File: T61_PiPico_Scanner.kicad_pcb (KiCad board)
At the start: 2 copper layers, 60 x 45 mm, 36 parts, among them J101 GND, J102 VBUS, J103 EXT5V, J105 GND, J106 PWRSWITCH, J107 AA01B-S040VA1, Q101 2N7002, Q102 2N7002, Q103 DMG2305UX, U101 Pico

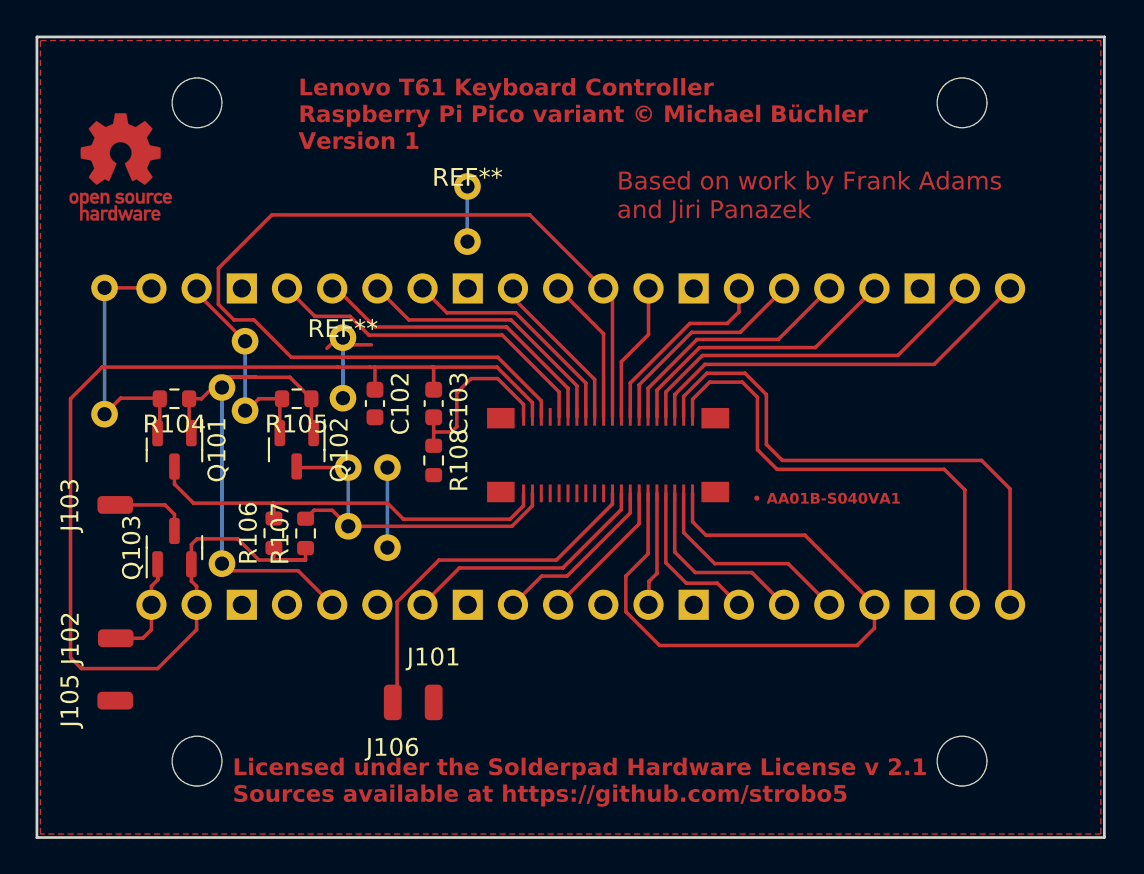
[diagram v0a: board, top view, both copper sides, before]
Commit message: rev 1.1: swap PS/2 clk and data for QMK's RP2040 PIO implementation
The only two boards with the wrong order were fixed manually.
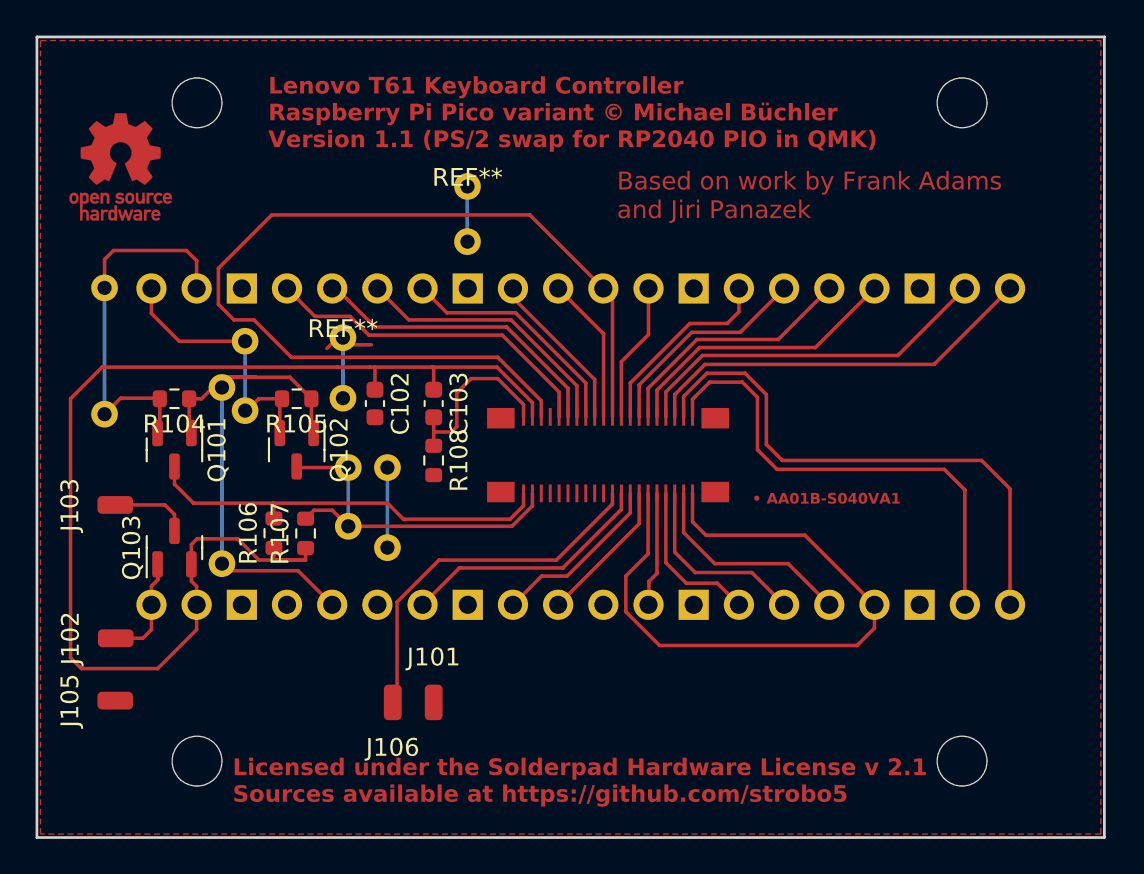
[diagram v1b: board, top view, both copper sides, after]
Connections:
- U101 pad 1: /TP4CLK_3V3 -> /TP4DATA_3V3
- U101 pad 2: /TP4DATA_3V3 -> /TP4CLK_3V3
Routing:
- net /TP4CLK_3V3: track 15.1 -> 21.8 mm
- net /TP4DATA_3V3: track 12.3 -> 16.0 mm
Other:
- board text added: "Lenovo T61 Keyboard Controller Raspberry Pi Pico variant © Michael Büchler Version 1.1 (PS/2 swap for RP2040 PIO in QMK)"
- board text removed: "Lenovo T61 Keyboard Controller Raspberry Pi Pico variant © Michael Büchler Version 1"
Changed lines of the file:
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@@
       (stroke (width 0.12) (type solid)) (layer "B.Fab"))
     (pad "1" thru_hole oval (at -8.89 24.13 270) (size 1.7 1.7) (drill 1.02) (layers "*.Cu" "*.Mask")
-      (net 41 "/TP4CLK_3V3") (pinfunction "GPIO0") (pintype "bidirectional"))
+      (net 42 "/TP4DATA_3V3") (pinfunction "GPIO0") (pintype "bidirectional"))
     (pad "2" thru_hole oval (at -8.89 21.59 270) (size 1.7 1.7) (drill 1.02) (layers "*.Cu" "*.Mask")
-      (net 42 "/TP4DATA_3V3") (pinfunction "GPIO1") (pintype "bidirectional"))
+      (net 41 "/TP4CLK_3V3") (pinfunction "GPIO1") (pintype "bidirectional"))
     (pad "3" thru_hole rect (at -8.89 19.05 270) (size 1.7 1.7) (drill 1.02) (layers "*.Cu" "*.Mask")
       (net 5 "GND") (pinfunction "GND") (pintype "power_in"))
@@
   (gr_line (start 118 128.295358) (end 118 83.295358)
     (stroke (width 0.1524) (type solid)) (layer "Edge.Cuts"))
-  (gr_text "Lenovo T61 Keyboard Controller\nRaspberry Pi Pico variant © Michael Büchler\nVersion 1" (at 132.7 89.7) (layer "F.Cu" knockout)
+  (gr_text "Lenovo T61 Keyboard Controller\nRaspberry Pi Pico variant © Michael Büchler\nVersion 1.1 (PS/2 swap for RP2040 PIO in QMK)" (at 131 89.6) (layer "F.Cu" knockout)
     (effects (font (size 0.93472 0.93472) (thickness 0.186944) bold) (justify left bottom))
   )
@@
   (segment (start 133.425 103.632) (end 132.218 102.425) (width 0.2) (layer "F.Cu") (net 40))
   (segment (start 128.4 112.9) (end 128.4 103) (width 0.2) (layer "B.Cu") (net 40))
-  (segment (start 123.90004 97.4) (end 124.18427 97.68423) (width 0.2) (layer "F.Cu") (net 41))
+  (segment (start 126.976 97.676) (end 126.976 97.4325) (width 0.2) (layer "F.Cu") (net 41))
   (segment (start 124.905 105.442) (end 124.905 103.632) (width 0.2) (layer "F.Cu") (net 41))
   (segment (start 121.8 104.5) (end 122.7 103.6) (width 0.2) (layer "F.Cu") (net 41))
-  (segment (start 121.8 97.4) (end 123.90004 97.4) (width 0.2) (layer "F.Cu") (net 41))
+  (segment (start 121.8 97.4) (end 121.8 95.8) (width 0.2) (layer "F.Cu") (net 41))
+  (segment (start 122.3 95.3) (end 126.4 95.3) (width 0.2) (layer "F.Cu") (net 41))
+  (segment (start 121.8 95.8) (end 122.3 95.3) (width 0.2) (layer "F.Cu") (net 41))
   (segment (start 124.78 105.567) (end 124.905 105.442) (width 0.2) (layer "F.Cu") (net 41))
+  (segment (start 126.4 95.3) (end 126.976 95.876) (width 0.2) (layer "F.Cu") (net 41))
+  (segment (start 126.9 97.00504) (end 126.72427 97.18077) (width 0.2) (layer "F.Cu") (net 41))
   (segment (start 122.7 103.6) (end 124.873 103.6) (width 0.2) (layer "F.Cu") (net 41))
   (segment (start 124.873 103.6) (end 124.905 103.632) (width 0.2) (layer "F.Cu") (net 41))
+  (segment (start 126.976 95.876) (end 126.976 97.4325) (width 0.2) (layer "F.Cu") (net 41))
   (segment (start 121.8 104.5) (end 121.8 97.4) (width 0.2) (layer "B.Cu") (net 41))
   (segment (start 129.7 104.3) (end 129.8 104.3) (width 0.2) (layer "F.Cu") (net 42))
+  (segment (start 123.90004 97.4) (end 124.18427 97.68423) (width 0.2) (layer "F.Cu") (net 42))
   (segment (start 131.775 103.632) (end 131.65 103.757) (width 0.2) (layer "F.Cu") (net 42))
-  (segment (start 126.976 97.676) (end 126.976 97.4325) (width 0.2) (layer "F.Cu") (net 42))
   (segment (start 131.65 103.757) (end 131.65 105.5625) (width 0.2) (layer "F.Cu") (net 42))
   (segment (start 129.8 104.3) (end 130.468 103.632) (width 0.2) (layer "F.Cu") (net 42))
+  (segment (start 124.436 98.836) (end 124.436 97.4325) (width 0.2) (layer "F.Cu") (net 42))
+  (segment (start 126 100.4) (end 124.436 98.836) (width 0.2) (layer "F.Cu") (net 42))
   (segment (start 130.468 103.632) (end 131.775 103.632) (width 0.2) (layer "F.Cu") (net 42))
-  (segment (start 129.7 100.4) (end 126.976 97.676) (width 0.2) (layer "F.Cu") (net 42))
+  (segment (start 129.7 100.4) (end 126 100.4) (width 0.2) (layer "F.Cu") (net 42))
   (segment (start 129.7 104.3) (end 129.7 100.4) (width 0.2) (layer "B.Cu") (net 42))
   (zone (net 0) (net_name "") (layer "F.Cu") (name "kbcon_nofill") (hatch edge 0.5)
